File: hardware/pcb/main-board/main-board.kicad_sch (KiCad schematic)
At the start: 48 parts, among them J1 USB-C, J10 CH552G_KEYBOARD_MCU, J11 KEYBOARD_BACKLIGHT_LEDS, J12 SPEAKER_1W_8OHM, J2 BATT_2x18650_PARALLEL, J3 BOOT0_OVERRIDE_JUMPER, J4 SWD_DEBUG, J5 MICROSD, J6 CR2032_HOLDER, J7 U.FL, J8 SMA_EDGE, J9 RA8875_DISPLAY_MODULE, Q1 2N7002, SW1 PWR_KEY, SW2 RESET, U1 MCP73831-2-OT, U10 PAM8403D, U2 IP5306, U3 AMS1117-3.3, U4 AMS1117-3.3, U5 GD32VF103CCT6, U6 W25Q64JVSSIQ, U7 23LC1024, U8 DS3231M, U9 ESP32-C3-MINI-1U, Y1 8MHz

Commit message: hardware: pre-fab design review of the Main Board, REV 0.7
Ran the design-review pass the Project Status table has been calling the
next step. Four findings on the board and one on the tooling.

Reference-designator drift. build_schematic.py auto-numbered refdes by
call order while build_pcb.py's PLACEMENT dict is keyed by refdes, so
adding the IP5306's inductor and snubber (615f5d2) renumbered every
later R and C by +1 and silently built a dozen parts into each other's
board positions. Measured on the committed board: the 8MHz crystal's
20pF load caps were 51mm and 34mm from the crystal, the IP5306's 22uF
snubber and VOUT caps were ~50mm from the IC, the audio filter's R and C
were 61mm and 70mm from the amplifier. Crystal load caps that far from
their crystal do not work -- this was a dead board that looked fine.

Fixed on both sides: all 48 components now pass an explicit ref= and
schematic.py's place() refuses to place anything without one, so refdes
is a declaration rather than a side effect of file order; and PLACEMENT
entries carry the expected component value, checked against the netlist
before anything is placed. build_pcb.py also now fails on courtyard
overlaps and on PLACEMENT entries not present in the netlist.

The IP5306 switching loop. Independent of the drift above, the inductor
commit placed L1 63mm from U2 with the VOUT cap 68mm away, in the open
band below the MCU. A 1uH boost converter's SW-node loop area is set by
exactly that distance. L1, the RC snubber and the VOUT cap now sit tight
around U2, whose BAT/SW/VOUT pins are all on its right-hand side; SW1
moved to the MCU column to make room, being a momentary switch on a
static input.

Trace widths. Everything was routed at the 0.2mm default including the
2.4A boost path, flagged for review when the inductor was added.
Netclasses now live in main-board.kicad_pro, written by build_pcb.py
before the board goes to the autorouter: 0.8mm for /VBATT and
/IP5306_SW, 0.4mm for +5V and VBUS, sized per IP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
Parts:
- C1, C2: value 22uF -> 20pF; footprint Capacitor_SMD:C_0805_2012Metric -> Capacitor_SMD:C_0603_1608Metric
- C3: value 20pF -> 100nF
- C4: value 20pF -> 22uF; footprint Capacitor_SMD:C_0603_1608Metric -> Capacitor_SMD:C_0805_2012Metric
- C5: value 100nF -> 22uF; footprint Capacitor_SMD:C_0603_1608Metric -> Capacitor_SMD:C_0805_2012Metric
- R11: value 4.7k -> 10k
- R13: value 10k -> 1k
- R14: value 1k -> 0.5R
- R5: value 0.5R -> 1k
- R6: value 1k -> 10k
- R9: value 10k -> 4.7k
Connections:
- net +3V3_MCU: now also R6.2, R9.2; no longer R11.2, R7.2
- net +3V3_RF: now also R11.2; no longer R13.2
- net +5V: now also C5.1, R5.1; no longer C2.1, R6.1
- net AUDIO_IN: now also C3.1, R13.2; no longer C5.1, R14.2
- net AUDIO_PWM: now also R13.1; no longer R14.1
- net BATT_LED1_R: now also R5.2; no longer R6.2
- net BOOT0: now also R7.1; no longer R8.1
- net BOOT1: now also R8.1; no longer R9.1
- net ESP_EN: now also R11.1; no longer R12.1
- net ESP_IO9: now also R12.1; no longer R13.1
- net GND: now also R7.2; no longer R9.2
- net I2C1_SCL: now also R9.1; no longer R10.1
- net I2C1_SDA: now also R10.1; no longer R11.1
- net IP5306_SW: now also R14.1; no longer R5.1
- net NRST: now also R6.1; no longer R7.1
- net OSC_IN: now also C1.1; no longer C3.1
- net OSC_OUT: now also C2.1; no longer C4.1
- net SNUBBER_MID: now also C4.1, R14.2; no longer C1.1, R5.2

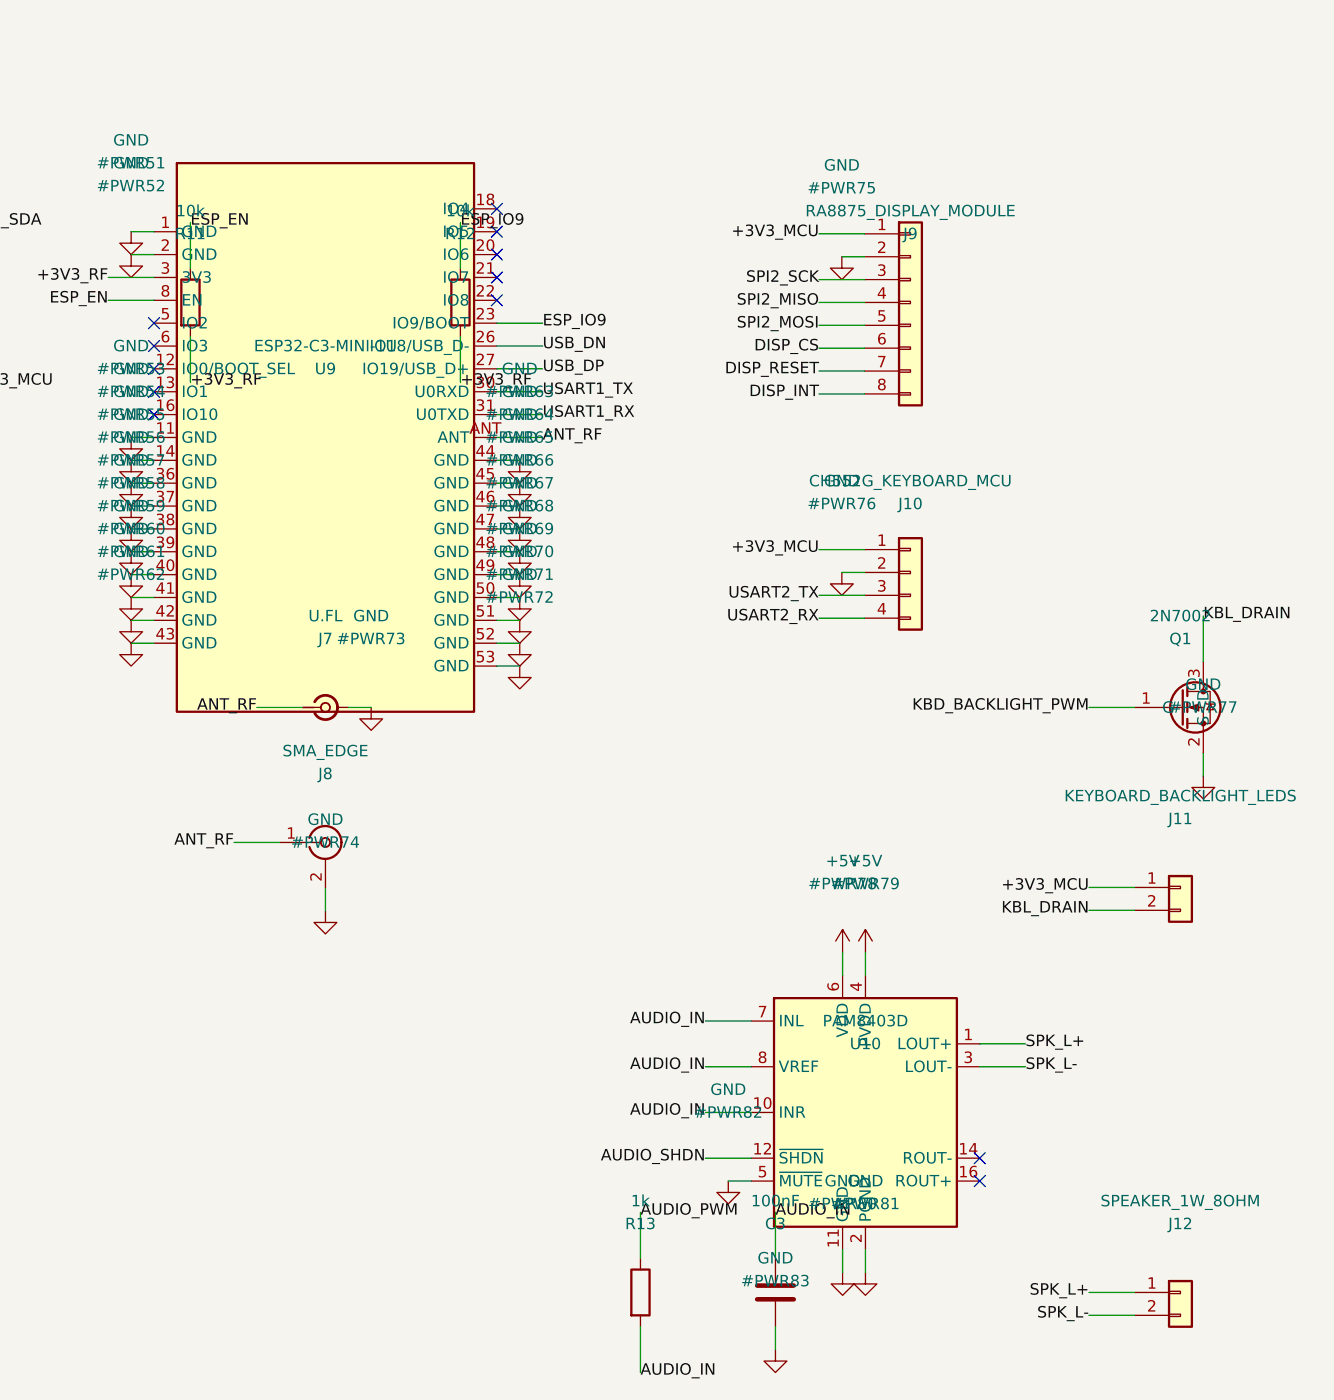
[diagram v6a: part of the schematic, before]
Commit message: hardware: remove the Main Board's antenna path, fix the stitching grid
This pass set out to do the item that headed the Main Board's "What's not
done yet": controlled-impedance layout for the 2.4GHz antenna path. There
is no antenna path. `/ANT_RF` has no `U9` pad on it -- the net was two
connectors wired to each other, with nothing driving them.

The ESP32-C3-MINI-1U does not bring its radio out to a castellated pad.
Datasheet v2.2 Table 3-1 lists all 53: pins 1, 2, 11, 14 and 36-53 are
GND, the rest are 3V3, EN and IO. The radio leaves through the antenna
jack mounted on the module -- that is what the "U" in -1U means. So:

- build_library.py's symbol carried a pin whose *number* was the string
  "ANT", matching no pad in the footprint. KiCad ties pins to pads by
  number, so a number matching nothing contributes nothing, and the
  netlist produced a two-connector net rather than an error.
- J7 was a second, board-mounted U.FL duplicating the module's own. The
  schematic comment beside it said as much ("U.FL pad on the
  ESP32-C3-MINI-1U module itself") and it was placed on the PCB anyway.
- The J7->J8 trace was therefore 19mm of 0.2mm copper between two
  connectors -- the net an RF review would have been asked to match.
- An edge-mount SMA cannot be reached by a pigtail in any case: its
  centre pin is a board pad. bom.md items 13 and 14 specified exactly
  that pair, which cannot be assembled as written.
- And the pigtail was the wrong connector generation. Section 10.2
  specifies the module's jack as the third generation -- Hirose W.FL,
  I-PEX MHF III, Amphenol AMC, body 2.05 x 1.7 x 1.40mm (Figure 10-3).
  U.FL / MHF I is the first generation, ~2.6mm, and does not mate.

J7, J8, /ANT_RF and the invented ANT pin are gone from the symbol, the
schematic, PLACEMENT and the board. The antenna is a cable assembly and a
case feature: MHF III pigtail from the module's own jack to a bulkhead
SMA in the enclosure wall. That closes the RF layout gap by removing it --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
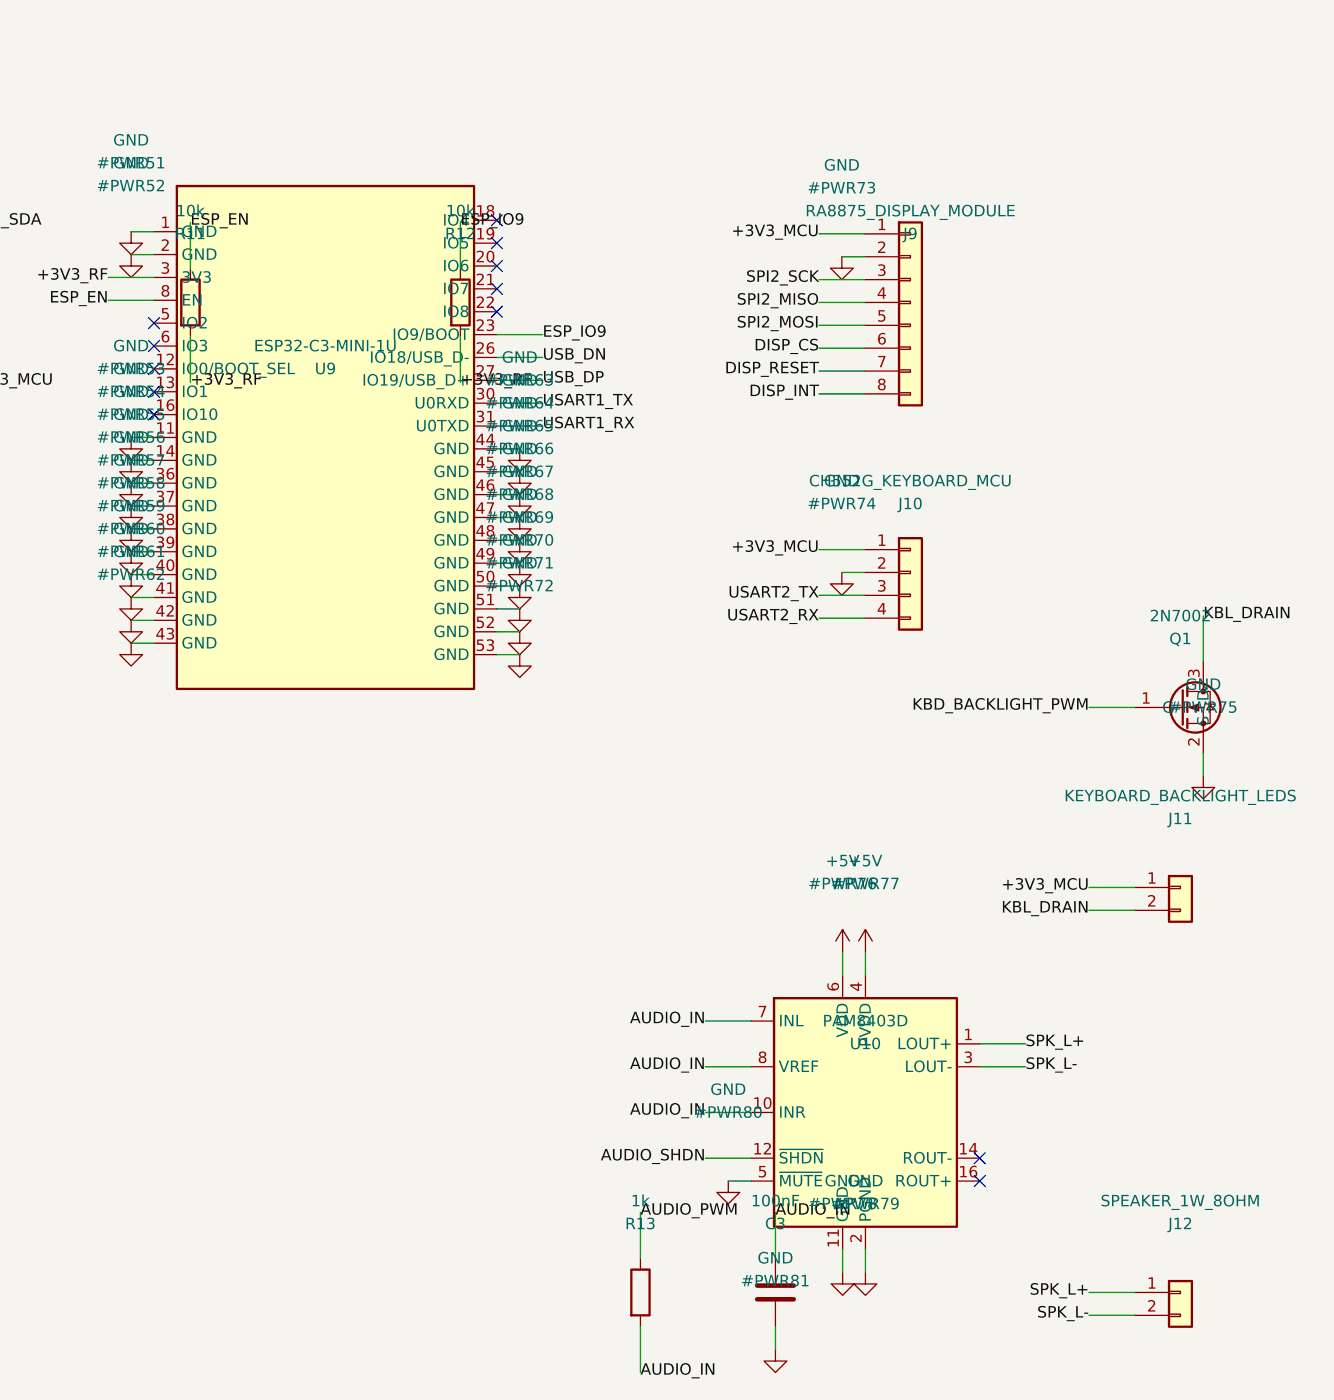
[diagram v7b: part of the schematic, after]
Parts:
- removed J7: U.FL, Connector_Coaxial:U.FL_Molex_MCRF_73412-0110_Vertical, symbol Connector:Conn_Coaxial_Small
- removed J8: SMA_EDGE, Connector_Coaxial:SMA_Amphenol_132289_EdgeMount, symbol Connector:Conn_Coaxial
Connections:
- removed net ANT_RF: U9.ANT
